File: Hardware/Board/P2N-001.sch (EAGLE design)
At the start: 37 parts, among them IC1 4053N, IC2 LTC485N, IC3 74LS07N, IC4 LTC485N, K1 G5V1, T1 2SC1815

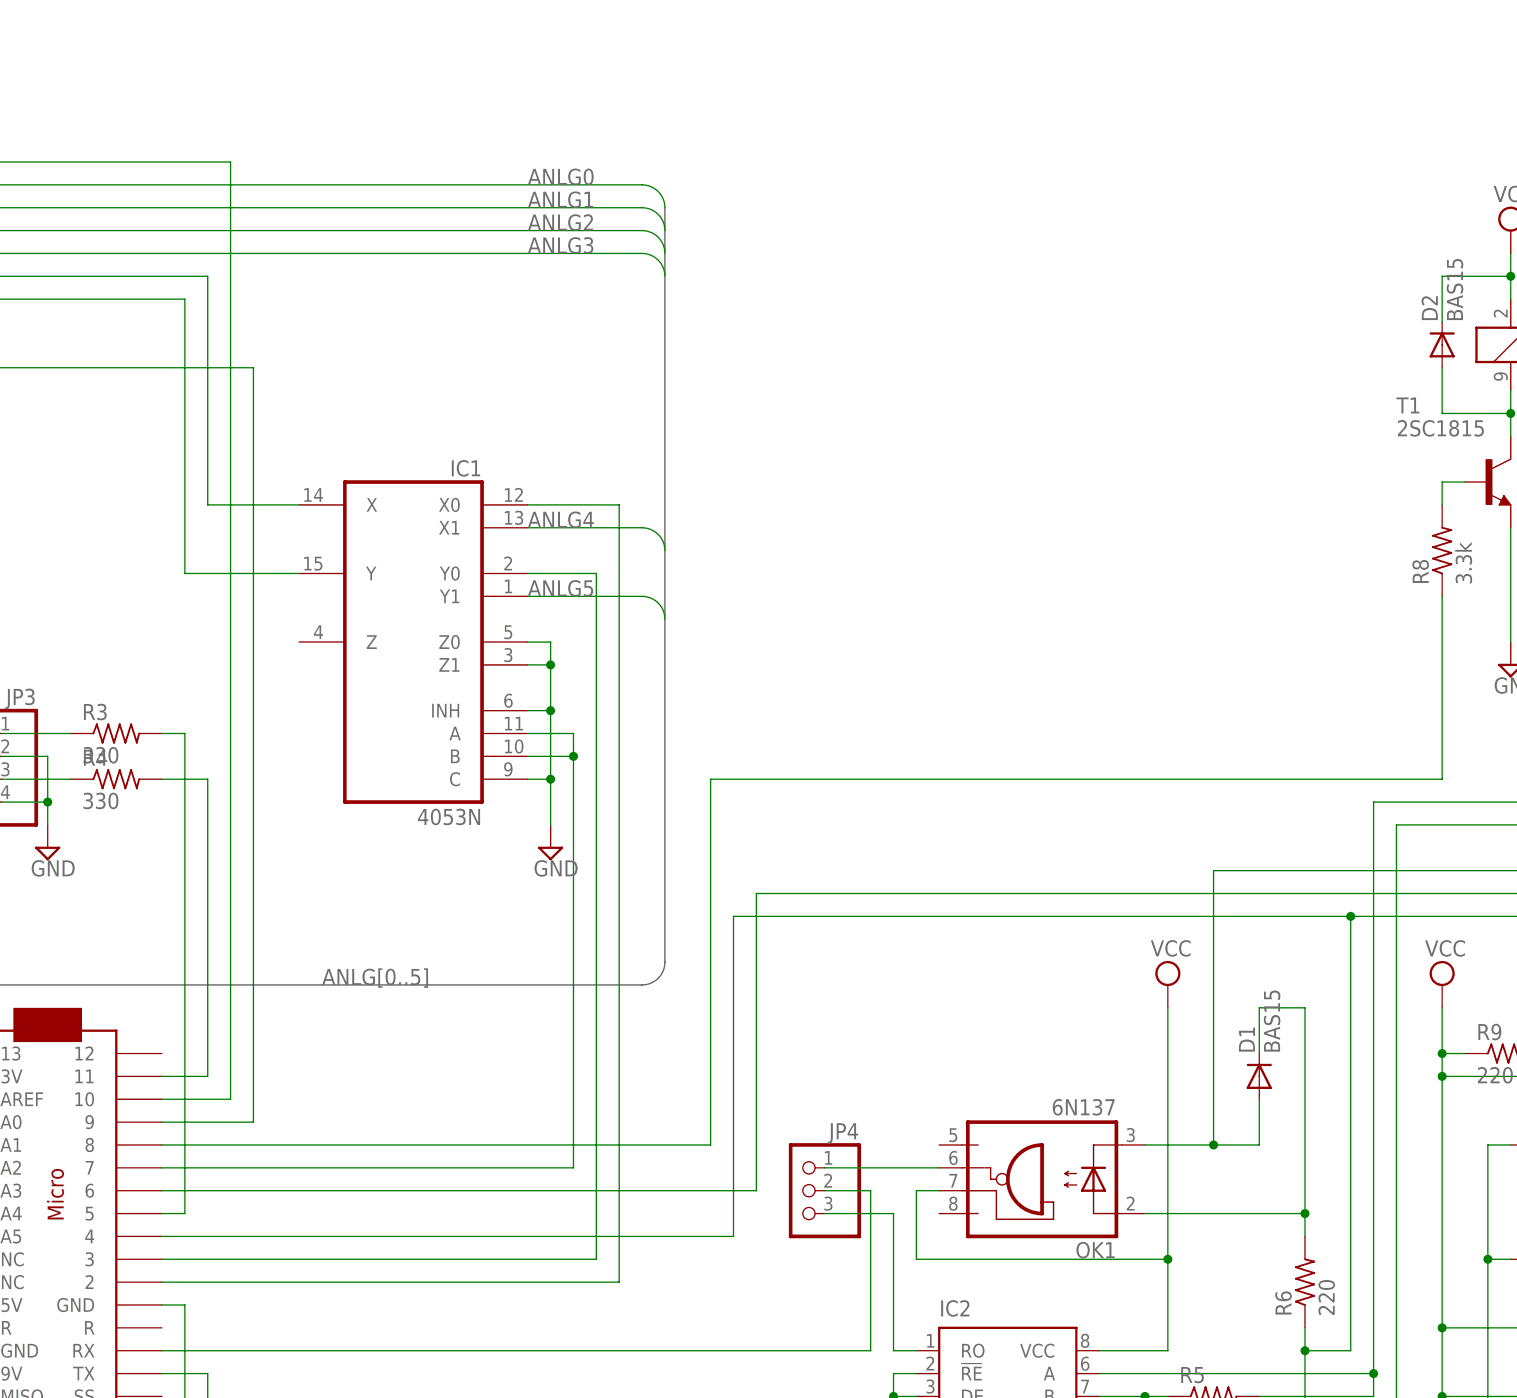
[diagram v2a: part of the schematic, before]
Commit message: Canceled change of XMIDI layout.
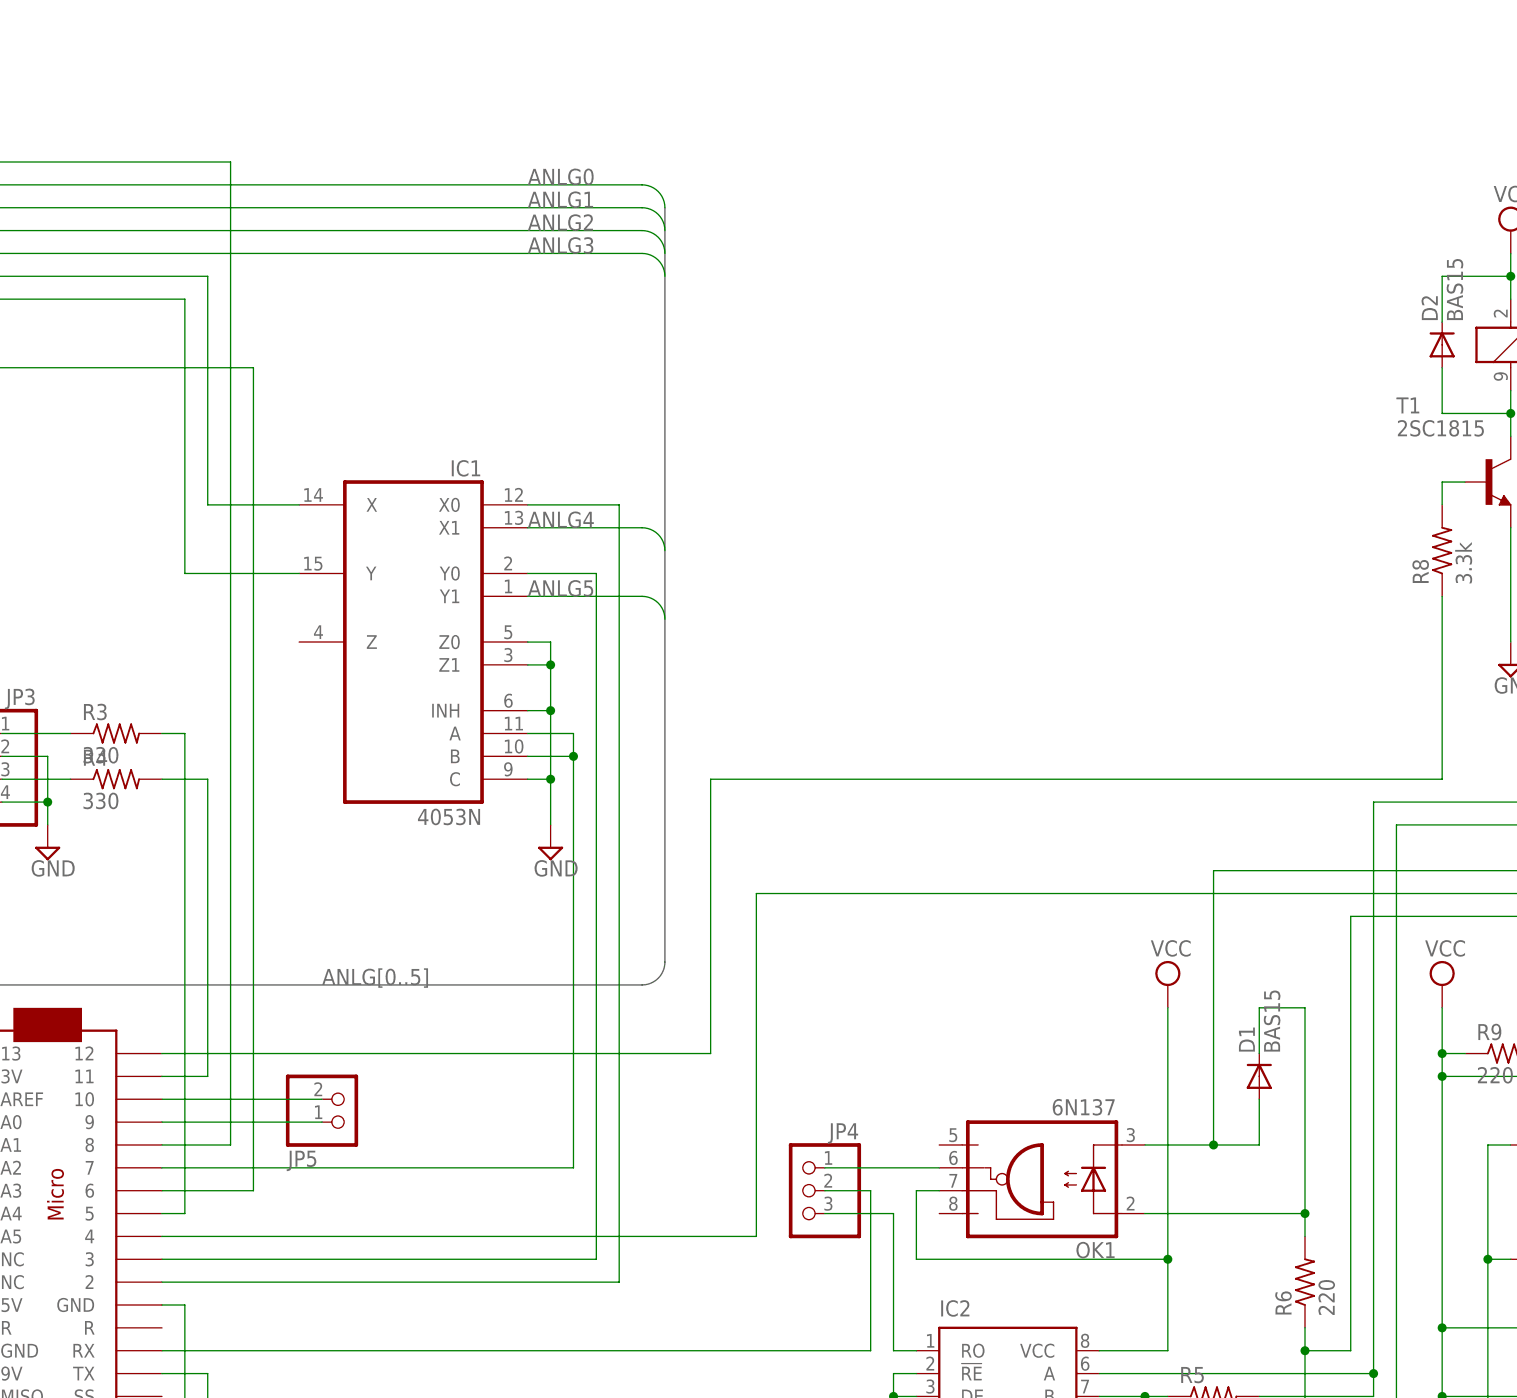
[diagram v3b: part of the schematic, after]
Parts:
- added JP5: (no value), pinhead:PINHD-1X2
- CN1: device jst-ph:B4B-PH-K-S -> jst-ph:S4B-PH-K-S
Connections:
- new net N$31: JP5.2, MC1.10
- new net N$32: JP5.1, MC1.9
- net MIDI14: no longer MC1.4
- net N$22: now also MC1.12; no longer MC1.8
- net N$24: now also MC1.8; no longer MC1.10
- net N$27: now also MC1.6; no longer MC1.9
- net N$9: now also MC1.4; no longer MC1.6
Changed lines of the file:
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@@
 <part name="SUPPLY21" library="supply2" deviceset="VCC" device=""/>
 <part name="K1" library="relay" deviceset="G5V1" device=""/>
-<part name="CN1" library="jst-ph" deviceset="B4B-PH-*" device="K-S"/>
+<part name="CN1" library="jst-ph" deviceset="S4B-PH-*" device="K-S"/>
 <part name="R3" library="resistor" deviceset="R-US_" device="0204/5" value="330"/>
 <part name="R4" library="resistor" deviceset="R-US_" device="0204/5" value="330"/>
 <part name="SUPPLY6" library="supply2" deviceset="GND" device=""/>
 <part name="JP3" library="pinhead" deviceset="PINHD-1X4" device=""/>
+<part name="JP5" library="pinhead" deviceset="PINHD-1X2" device=""/>
 </parts>
 <sheets>
@@
 <instance part="SUPPLY6" gate="GND" x="58.42" y="93.98"/>
 <instance part="JP3" gate="A" x="50.8" y="101.6" rot="MR0"/>
+<instance part="JP5" gate="G$1" x="91.44" y="66.04" rot="MR180"/>
 </instances>
 <busses>
@@
 <wire x1="307.34" y1="119.38" x2="294.64" y2="119.38" width="0.1524" layer="91"/>
 <junction x="198.12" y="38.1"/>
-<wire x1="203.2" y1="86.36" x2="134.62" y2="86.36" width="0.1524" layer="91"/>
-<wire x1="134.62" y1="86.36" x2="134.62" y2="50.8" width="0.1524" layer="91"/>
-<pinref part="MC1" gate="G$1" pin="4"/>
-<wire x1="134.62" y1="50.8" x2="71.12" y2="50.8" width="0.1524" layer="91"/>
-<junction x="203.2" y="86.36"/>
 </segment>
 </net>
@@
 <net name="N$9" class="0">
 <segment>
-<pinref part="MC1" gate="G$1" pin="6"/>
-<wire x1="71.12" y1="55.88" x2="137.16" y2="55.88" width="0.1524" layer="91"/>
-<wire x1="137.16" y1="55.88" x2="137.16" y2="88.9" width="0.1524" layer="91"/>
 <wire x1="137.16" y1="88.9" x2="266.7" y2="88.9" width="0.1524" layer="91"/>
 <wire x1="266.7" y1="88.9" x2="266.7" y2="132.08" width="0.1524" layer="91"/>
 <pinref part="SV1" gate="1" pin="3"/>
 <wire x1="266.7" y1="132.08" x2="279.4" y2="132.08" width="0.1524" layer="91"/>
+<wire x1="137.16" y1="88.9" x2="137.16" y2="50.8" width="0.1524" layer="91"/>
+<pinref part="MC1" gate="G$1" pin="4"/>
+<wire x1="137.16" y1="50.8" x2="71.12" y2="50.8" width="0.1524" layer="91"/>
 </segment>
 </net>
@@
 <net name="N$22" class="0">
 <segment>
-<pinref part="MC1" gate="G$1" pin="8"/>
-<wire x1="71.12" y1="60.96" x2="132.08" y2="60.96" width="0.1524" layer="91"/>
-<wire x1="132.08" y1="60.96" x2="132.08" y2="101.6" width="0.1524" layer="91"/>
 <wire x1="132.08" y1="101.6" x2="213.36" y2="101.6" width="0.1524" layer="91"/>
 <pinref part="R8" gate="G$1" pin="1"/>
 <wire x1="213.36" y1="101.6" x2="213.36" y2="121.92" width="0.1524" layer="91"/>
+<pinref part="MC1" gate="G$1" pin="12"/>
+<wire x1="71.12" y1="71.12" x2="132.08" y2="71.12" width="0.1524" layer="91"/>
+<wire x1="132.08" y1="71.12" x2="132.08" y2="101.6" width="0.1524" layer="91"/>
 </segment>
 </net>
@@
 <wire x1="33.02" y1="170.18" x2="33.02" y2="144.78" width="0.1524" layer="91"/>
 <wire x1="33.02" y1="170.18" x2="78.74" y2="170.18" width="0.1524" layer="91"/>
-<wire x1="78.74" y1="170.18" x2="78.74" y2="66.04" width="0.1524" layer="91"/>
-<pinref part="MC1" gate="G$1" pin="10"/>
-<wire x1="78.74" y1="66.04" x2="71.12" y2="66.04" width="0.1524" layer="91"/>
 <junction x="33.02" y="170.18"/>
+<wire x1="78.74" y1="170.18" x2="78.74" y2="60.96" width="0.1524" layer="91"/>
+<pinref part="MC1" gate="G$1" pin="8"/>
+<wire x1="78.74" y1="60.96" x2="71.12" y2="60.96" width="0.1524" layer="91"/>
 </segment>
 </net>
@@
 <wire x1="30.48" y1="172.72" x2="30.48" y2="147.32" width="0.1524" layer="91"/>
 <wire x1="30.48" y1="147.32" x2="81.28" y2="147.32" width="0.1524" layer="91"/>
-<wire x1="81.28" y1="147.32" x2="81.28" y2="63.5" width="0.1524" layer="91"/>
-<pinref part="MC1" gate="G$1" pin="9"/>
-<wire x1="81.28" y1="63.5" x2="71.12" y2="63.5" width="0.1524" layer="91"/>
+<wire x1="81.28" y1="147.32" x2="81.28" y2="55.88" width="0.1524" layer="91"/>
+<pinref part="MC1" gate="G$1" pin="6"/>
+<wire x1="81.28" y1="55.88" x2="71.12" y2="55.88" width="0.1524" layer="91"/>
 </segment>
 </net>
@@
 </segment>
 </net>
+<net name="N$31" class="0">
+<segment>
+<pinref part="MC1" gate="G$1" pin="10"/>
+<pinref part="JP5" gate="G$1" pin="2"/>
+<wire x1="71.12" y1="66.04" x2="88.9" y2="66.04" width="0.1524" layer="91"/>
+</segment>
+</net>
+<net name="N$32" class="0">
+<segment>
+<pinref part="MC1" gate="G$1" pin="9"/>
+<pinref part="JP5" gate="G$1" pin="1"/>
+<wire x1="71.12" y1="63.5" x2="88.9" y2="63.5" width="0.1524" layer="91"/>
+</segment>
+</net>
